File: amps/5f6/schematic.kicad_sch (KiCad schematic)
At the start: 69 parts, among them T3 2R sec

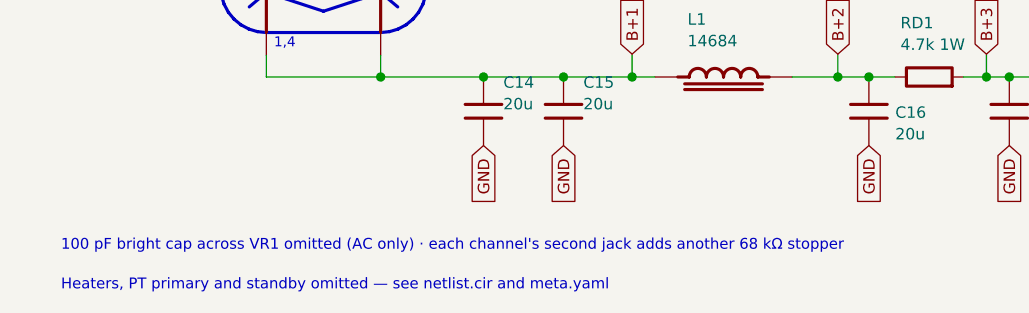
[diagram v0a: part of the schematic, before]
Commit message: Fix: schematic sheet notes no longer name repository files
Thirty-seven committed sheets rendered footnotes and section notes such as
"Heaters and PT primary omitted — see netlist.cir and meta.yaml" or
"excluded from netlist.cir (notes.md)" to visitors through KiCanvas. The
prose sweeps never counted sheets. Rewritten in the site's own words — the
netlist, the sources list, the circuit story, the parts list, the board
drawing — in 59 strings across 33 draw scripts, keeping every technical
claim as it was; the three tone sheets (6G4, 6G5, 6G6-B) are under repair
elsewhere and keep theirs for now. The sweep touched only strings passed to
the sheet's note, text, caption and footnote calls, never a path or a value.

Gates: check_schematics 40/0, connectivity 0 isolated pins;
verify_schematic_nets 40 clean; only the regenerated sheets and their served
copies changed.

Co-Authored-By: Claude Fable 5.1 <noreply@anthropic.com>
Claude-Session: https://claude.ai/code/session_01KBMfdh37HmCL2iWcBiL5J1
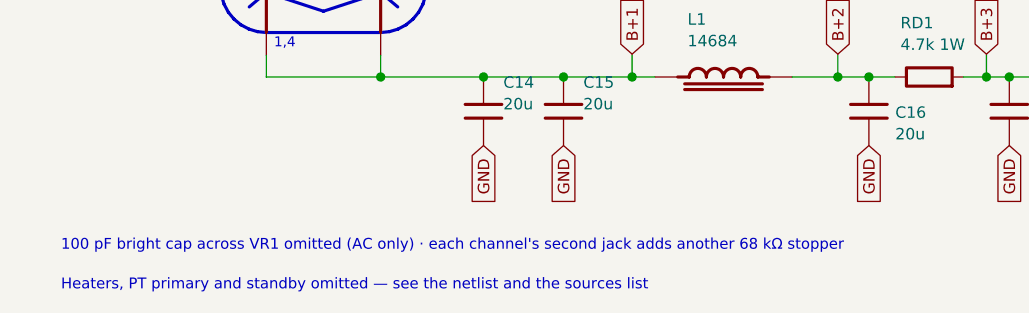
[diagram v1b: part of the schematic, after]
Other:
- note added: "Heaters, PT primary and standby omitted — see the netlist and the sources list"
- note removed: "Heaters, PT primary and standby omitted — see netlist.cir and meta.yaml"
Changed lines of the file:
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@@
   (text "100 pF bright cap across VR1 omitted (AC only) · each channel's second jack adds another 68 kΩ stopper" (at 12.7 142.856 0)
     (effects (font (size 1.2 1.2)) (justify left)))
-  (text "Heaters, PT primary and standby omitted — see netlist.cir and meta.yaml" (at 12.7 147.256 0)
+  (text "Heaters, PT primary and standby omitted — see the netlist and the sources list" (at 12.7 147.256 0)
     (effects (font (size 1.2 1.2)) (justify left)))
   (sheet_instances (path "/" (page "1")))

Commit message: Add: sheet<->board net-equivalence gate over every part, no netlist (survey + drift-gated worklist)
pipeline/verify_sheet_vs_board.py proves the schematic and the board layout
draw the SAME circuit over the ~1,280 BOM passives the DC netlist does not
model — the parts both existing equivalence gates skip by construction. The
two drawings are authored independently, so their net partitions are each
other's witness: <GND>, tube pins (through basing + the datasheet unit the
sheet states), pot wipers, jack contacts (cx:JACK T/S <-> J.tip/J.sleeve)
and declared net_map.leads anchor the partitions to each other; two-terminal
parts and pot ends resolve as unordered pairs by majority voting; a
section<->unit swap is searched for on every dual-section socket and
reported once. Heaters and the pilot lamp are excluded (check_heaters owns
them); every symbol class the board cannot name is listed in scope.

Declarations (docs/layout-schema.md): a sheet part the board neither places
nor wires must be covered by net_map.netlist_unplaced / series_bridge
(layout or sch_map — a bridged part the board does not place is compared
as one net, the conductor runs through it), a new per-part
net_map.not_on_board, or a new board-scope rule scope.not_drawn
(glob + why). A declaration covering nothing is a STALE DECLARATION.
No amp declares anything yet: that is a source-read job.

schematic_lib: a draw script that states `unit=` now emits it as a hidden
symbol property, Basing_unit, so the gate reads the unit off the sheet and
not the script (the script is the fallback, and the scope line says so).
Sheets drawn without unit= are byte-identical. NOT regenerated here: the
four sheets that state a unit (5e4a, 5f6, aa764, aa764-vibro) need
`draw_<id>.py` + sync-assets before the schematic-drift step of CI passes.

Found at HEAD 07dea48 (reference/sheet-board.yaml, --export), 40 amps,
38 with findings, 36 of them with both drawings claiming verified:
  SECTION-SWAP 25 sockets on 16 sheets, SPLIT 4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
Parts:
- V2A, V3A: Basing_unit (none) -> 2
- V2B, V3B: Basing_unit (none) -> 1
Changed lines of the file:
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@@
     (in_bom yes) (on_board yes)
     (property "Reference" "V2A" (at 83.3042 55.558 0) (effects (font (size 1.27 1.27)) (justify left)))
-    (property "Value" "12AX7" (at 83.3042 57.958 0) (effects (font (size 1.27 1.27)) (justify left))))
+    (property "Value" "12AX7" (at 83.3042 57.958 0) (effects (font (size 1.27 1.27)) (justify left)))
+    (property "Basing_unit" "2" (at 83.3042 60.358 0) (effects (font (size 1.27 1.27)) hide)))
   (wire (pts (xy 85.0488 55.278) (xy 87.5888 55.278))
     (stroke (width 0) (type default)))
@@
     (in_bom yes) (on_board yes)
     (property "Reference" "V2B" (at 116.449 48.878 0) (effects (font (size 1.27 1.27)) (justify left)))
-    (property "Value" "12AX7 CF" (at 116.449 51.278 0) (effects (font (size 1.27 1.27)) (justify left))))
+    (property "Value" "12AX7 CF" (at 116.449 51.278 0) (effects (font (size 1.27 1.27)) (justify left)))
+    (property "Basing_unit" "1" (at 116.449 53.678 0) (effects (font (size 1.27 1.27)) hide)))
   (wire (pts (xy 102.509 44.178) (xy 102.509 55.278))
     (stroke (width 0) (type default)))
@@
     (in_bom yes) (on_board yes)
     (property "Reference" "V3A" (at 176.139 31.878 0) (effects (font (size 1.27 1.27)) (justify left)))
-    (property "Value" "12AX7" (at 176.139 34.278 0) (effects (font (size 1.27 1.27)) (justify left))))
+    (property "Value" "12AX7" (at 176.139 34.278 0) (effects (font (size 1.27 1.27)) (justify left)))
+    (property "Basing_unit" "2" (at 176.139 36.678 0) (effects (font (size 1.27 1.27)) hide)))
   (wire (pts (xy 162.519 38.278) (xy 162.519 38.278))
     (stroke (width 0) (type default)))
@@
     (in_bom yes) (on_board yes)
     (property "Reference" "V3B" (at 158.234 72.558 0) (effects (font (size 1.27 1.27)) (justify left)))
-    (property "Value" "12AX7" (at 158.234 74.958 0) (effects (font (size 1.27 1.27)) (justify left))))
+    (property "Value" "12AX7" (at 158.234 74.958 0) (effects (font (size 1.27 1.27)) (justify left)))
+    (property "Basing_unit" "1" (at 158.234 77.358 0) (effects (font (size 1.27 1.27)) hide)))
   (wire (pts (xy 170.139 30.658) (xy 170.139 27.178))
     (stroke (width 0) (type default)))

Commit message: Fix: draw the 1 MΩ input grid leak on the jack-1 tip node, not the grid, on eight tweed/Champ sheets
Every tweed and Champ factory sheet hangs the 1 MΩ from the jack-1 tip
node (the node the jack-2 shorting contact also lands on) to ground, and
runs the 68 K stoppers from the jack tips to the grid. These eight sheets
drew the 1 MΩ on the GRID side of the stopper — one copy-pasted idiom in
four scripts and its cousins in four more; there is no shared helper, so
each script is fixed where it draws the block. The stopper is declared
DC-transparent (layout net_map.series_bridge), so the netlist sees one node
either way and verify_schematic_nets stays 40 clean; the sheet-vs-board
gate, which compares the drawings to each other, drops all twelve
MISPLACED findings (RG1/RG2 on 5e4a, 5e5a, 5f4, 5f6; R3 on 5f2a, aa764,
aa764-vibro; R1 on 5f1). 5f10's jack chain is a separate task.

Crops read: 5e4a-RG1-RG2-input.png, 5e5a-RG1-RG2-input.png,
5f4-RG1-input.png, 5f6-RG1-RG2-input.png, 5f2a-R3-input.png,
5f1-R1-input.png, aa764-R3-input.png, aa764-vibro-R3-input.png — each
prints "1 MEG." from the jack-1 tip to ground with the 68K pair to the grid.

Geometry: the four two-channel sheets hang the leak from the stopper's
jack-side pin; 5f1 drops it from the INPUT line; 5f2a and the two Champs
stand it upward off the jack-1 line because the jack-2 line runs 8–12 mm
below. Previews read cleanly. The circuit stories already say the leaks
mount at the jacks, so no prose changed.

Gates: check_schematics 40/0 (0 isolated), verify_schematic_nets 40
clean, validate/value-consistency/era-values clean, regenerate-all leaves
every other sheet byte-identical. verify_sheet_vs_board misplaced 98 -> 86.

Co-Authored-By: Claude Fable 5.1 <noreply@anthropic.com>
Claude-Session: https://claude.ai/code/session_01KBMfdh37HmCL2iWcBiL5J1
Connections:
- net BRIGHT: now also RG1.1
- net NORMAL: now also RG2.1
- net at R2s.2, V1B.2 (G): no longer RG2.1
- net at R1s.2, V1A.2 (G): no longer RG1.1
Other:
- moved on the sheet: RG1, RG2
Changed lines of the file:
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@@
   (wire (pts (xy 31.7088 38.278) (xy 35.5188 38.278))
     (stroke (width 0) (type default)))
-  (junction (at 31.7088 38.278) (diameter 1.032) (color 0 0 0 0))
-  (symbol (lib_id "cx:R") (at 31.7088 42.088 0) (unit 1)
+  (junction (at 24.0888 38.278) (diameter 1.032) (color 0 0 0 0))
+  (symbol (lib_id "cx:R") (at 24.0888 42.088 0) (unit 1)
     (in_bom yes) (on_board yes)
-    (property "Reference" "RG1" (at 33.9088 38.888 0) (effects (font (size 1.27 1.27)) (justify left)))
-    (property "Value" "1M" (at 33.9088 41.288 0) (effects (font (size 1.27 1.27)) (justify left))))
-  (global_label "GND" (shape input) (at 31.7088 45.898 270)
+    (property "Reference" "RG1" (at 26.2888 42.088 0) (effects (font (size 1.27 1.27)) (justify left)))
+    (property "Value" "1M" (at 26.2888 44.488 0) (effects (font (size 1.27 1.27)) (justify left))))
+  (global_label "GND" (shape input) (at 24.0888 45.898 270)
     (effects (font (size 1.27 1.27)) (justify right)))
   (wire (pts (xy 43.1388 30.658) (xy 43.1388 27.178))
@@
   (wire (pts (xy 31.7088 72.278) (xy 35.5188 72.278))
     (stroke (width 0) (type default)))
-  (junction (at 31.7088 72.278) (diameter 1.032) (color 0 0 0 0))
-  (symbol (lib_id "cx:R") (at 31.7088 76.088 0) (unit 1)
+  (junction (at 24.0888 72.278) (diameter 1.032) (color 0 0 0 0))
+  (symbol (lib_id "cx:R") (at 24.0888 76.088 0) (unit 1)
     (in_bom yes) (on_board yes)
-    (property "Reference" "RG2" (at 33.9088 72.888 0) (effects (font (size 1.27 1.27)) (justify left)))
-    (property "Value" "1M" (at 33.9088 75.288 0) (effects (font (size 1.27 1.27)) (justify left))))
-  (global_label "GND" (shape input) (at 31.7088 79.898 270)
+    (property "Reference" "RG2" (at 26.2888 76.088 0) (effects (font (size 1.27 1.27)) (justify left)))
+    (property "Value" "1M" (at 26.2888 78.488 0) (effects (font (size 1.27 1.27)) (justify left))))
+  (global_label "GND" (shape input) (at 24.0888 79.898 270)
     (effects (font (size 1.27 1.27)) (justify right)))
   (wire (pts (xy 43.1388 64.658) (xy 43.1388 61.178))

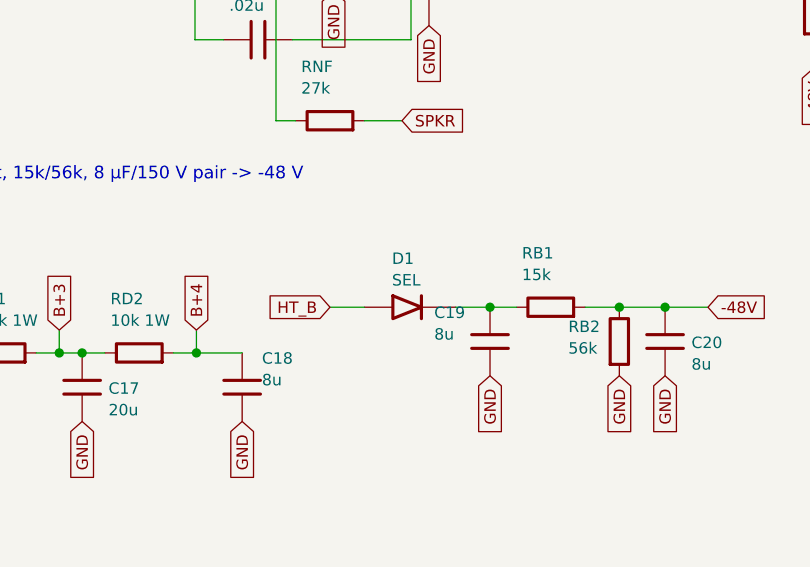
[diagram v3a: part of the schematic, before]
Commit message: Fix: 17 bias rectifiers and six HT diodes drawn backwards; the 6G6-B and 6G4 bias rows as their drawings show; AA1164 V4 units
Rectifier polarity has no gate. The netlists model every supply as an ideal
source, the sheet-vs-board check treats a two-terminal part as unordered, and
the boards' `cathode:` fields were copied from the sheets. Measured over all
68 diodes on 40 sheets: 18 negative-bias rectifiers had the cathode on the
negative node (a diode that way round would charge the node POSITIVE), and all
six 6G6-B HT diodes pointed away from B+. The printed negative bias on each of
those sheets falsifies the drawn orientation; the nine bias rectifiers already
right (AA1164, AA864, AB165, B15N, DR103, JTM100, M1959, M2204, 6G6-B) show
the idiom. Flipped: 5E4-A, 5E5-A, 5E6-A, 5F10, 5F4, 5F6, 5F6-A, 5F8-A, 5G9,
6G2, 6G3, 6G4, 6G5, AA964, AB763, AB763 Super, AB763 Twin, JTM45 (the
M1987's is with the Marshall board repair) and the 6G6-B's DR1-DR6. The
5F8-A board, which had copied its sheet, has the band moved to the tap side;
the other boards' bands are with the board-repair wave. A gate is next.

6G6-B bias. E-FB (6431x3364): the 1K 1W rises from TR1's SECOND secondary
terminal, a bias tap between the upper HT end and the grounded centre tap,
to the diode's + end. The sheet fed the diode from the HT end with the 1K
after it. T1 now carries its tap pin and the row reads tap -> 1K -> diode ->
-54 V. (The triage had read "HT end"; the native crop shows the tap.)

6G4 bias. A-FJ, read natively: tap -> rectifier -> 8 uF -> 10K -> the -55 V
node, which carries a second 8 uF and the 56K to ground as a bleeder. The
sheet fed the rectifier from an HT end, drew the 56K in series and carried
one capacitor. CBIAS2 joins the parts list, and RBIAS1's role now says
bleeder.

AA1164 V4. The K-FD sheet prints the phase inverter 7/6/8 and the tremolo
oscillator 2/1/3 (5554x4346); the sheet had them the other way round.

Gates: check_schematics 40/0 (+selftest), verify_schematic_nets 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
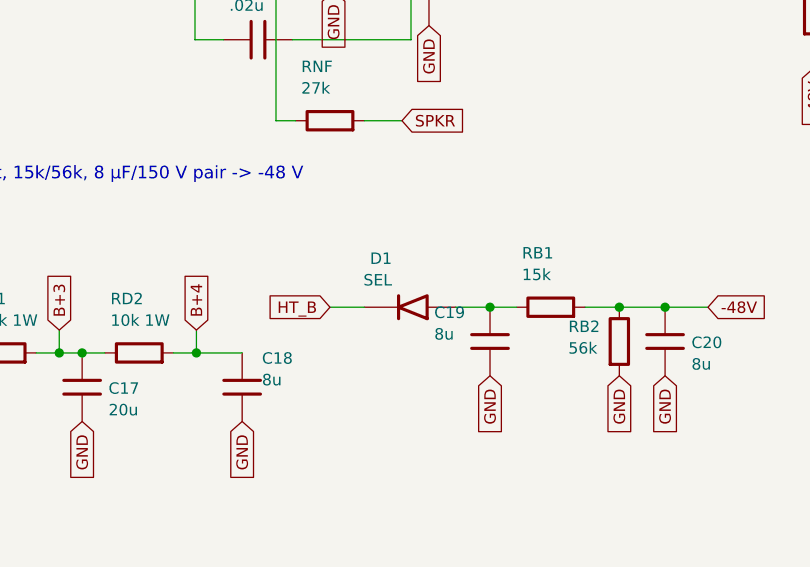
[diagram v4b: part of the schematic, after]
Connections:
- net HT_B: now also D1.2 (K); no longer D1.1 (A)
- net at C19.1, RB1.1: now also D1.1 (A); no longer D1.2 (K)
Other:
- moved on the sheet: D1
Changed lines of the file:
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@@
   (wire (pts (xy 145.609 118.998) (xy 149.419 118.998))
     (stroke (width 0) (type default)))
-  (symbol (lib_id "cx:DIODE_SS") (at 154.499 118.998 0) (unit 1)
+  (symbol (lib_id "cx:DIODE_SS") (at 154.499 118.998 180) (unit 1)
     (in_bom yes) (on_board yes)
     (property "Reference" "D1" (at 152.499 113.598 0) (effects (font (size 1.27 1.27)) (justify left)))

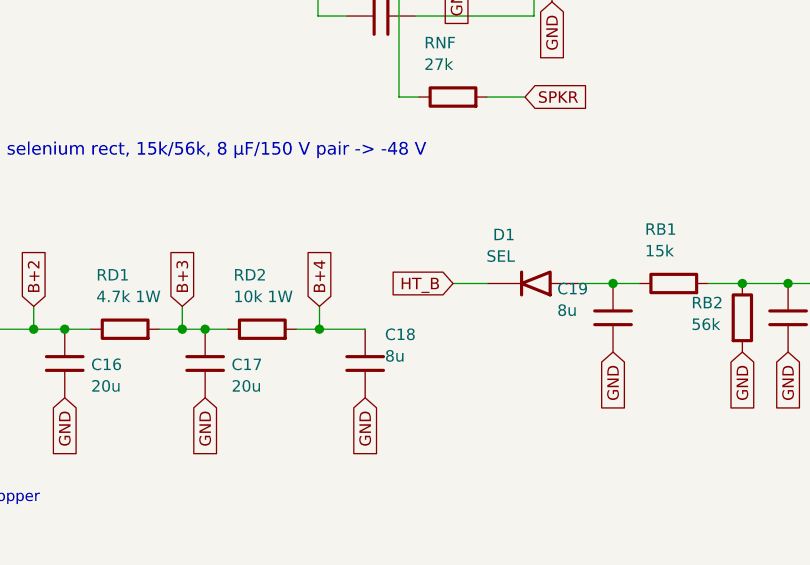
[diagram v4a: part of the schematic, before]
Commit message: Fix: the 5F6, 5F8-A and 5F6-A sheets fed the selenium bias rectifier from an HT end; it takes its own tap
All three factory schematics bring the bias feed down to its OWN winding terminal, between the upper HT end and the centre tap. It is not the HT end. At 3x zoom the vertical feed line crosses the upper "325 V AC" (5F8-A: "300 V AC") lead with no junction dot and ends on the next terminal down:
- 5F6 (F-EG) schematic page, crop (3560,3580)-(3900,3880), in the context of (3550,2850)-(4650,4100);
- 5F8-A (I-EG), native 6310x3506, crop (3250,2800)-(3800,3350);
- 5F6-A (I-EG), crop (3550,3500)-(4000,3950).
The layout pages agree. 5F6 crop (900,2200)-(2900,3800) and 5F8-A crop (600,1300)-(2400,2000) each draw a dedicated RED-BLUE transformer lead to SEL. RECT. "+", separate from the two RED HT leads that go to the rectifier plates.

So red-blue is a separate tap, as on the 6G6-B, and the sheets were the surface in error: each lettered D1's anode HT_B, putting the bias rectifier on the rectifier plate node. Each sheet now letters it HT_TAP. sch_map.yaml winding_labels declares HT_TAP: tap, so the UNFED RECTIFIER walk still sees D1 fed, and HT_B's note drops "also feeds bias rectifier D1". The 5F6 and 5F8-A boards, which wire PT.red-blue to D1, declare net_map.leads "<HT_TAP>": PT.red-blue. The 5F6-A board does not place D1 (a declared not_on_board), so it needs no lead.

Sheet-board: 5F6 misplaced [D1] -> [] (both drawings claim verified; it now PASSes), 5F8-A misplaced [D1] -> []. verify_schematic_nets PASS for all three, and 48/48 rectifiers fed. No netlist change: the bias supply is the ideal NBIAS source in every netlist. FW-19 P10c.

Co-Authored-By: Claude Opus 5.5 <noreply@anthropic.com>
Claude-Session: https://claude.ai/code/session_01KBMfdh37HmCL2iWcBiL5J1
Signed-off-by: AnalogMaker <theanalogmaker@gmail.com>
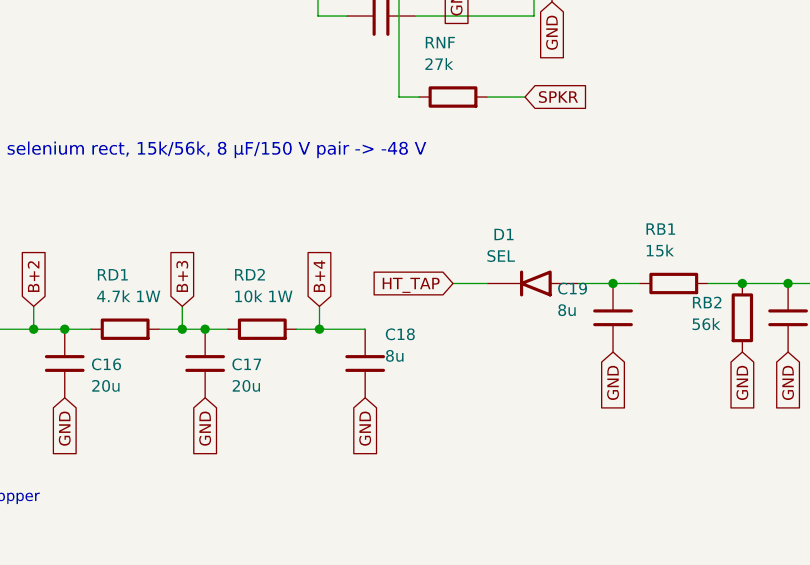
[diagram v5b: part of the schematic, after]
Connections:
- net HT_B: no longer D1.2 (K)
- new net HT_TAP: D1.2 (K)
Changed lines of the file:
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@@
   (global_label "GND" (shape input) (at 135.849 131.698 270)
     (effects (font (size 1.27 1.27)) (justify right)))
-  (global_label "HT_B" (shape input) (at 145.609 118.998 180)
+  (global_label "HT_TAP" (shape input) (at 145.609 118.998 180)
     (effects (font (size 1.27 1.27)) (justify right)))
   (wire (pts (xy 145.609 118.998) (xy 149.419 118.998))
